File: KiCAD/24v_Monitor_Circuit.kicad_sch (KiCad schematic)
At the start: 2 parts, among them U3 PC365NJ0000F

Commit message: Ran Annotation and ERC
Annotated and ran Electronics Rules Checker. Started assigning footprints and appropriate step files to said footprints. Added custom KiCAD library folder to Github.
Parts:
- R17: renamed from R3; value R -> 2.28kΩ
- renumbered U3 to U10
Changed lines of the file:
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@@
   (symbol (lib_id "power:+24V") (at 111.76 76.2 0) (unit 1)
     (in_bom yes) (on_board yes) (dnp no) (fields_autoplaced)
-    (property "Reference" "#PWR011" (at 111.76 80.01 0)
+    (property "Reference" "#PWR020" (at 111.76 80.01 0)
       (effects (font (size 1.27 1.27)) hide)
     )
@@
       (project "ColletAutoFeed_RelayBoard"
         (path "/603d0a2e-fca7-40af-8fa8-51b59d823d4d/3e3ccaf3-28fc-483d-ba21-ff253f5b1972"
-          (reference "#PWR011") (unit 1)
+          (reference "#PWR020") (unit 1)
         )
       )
@@
   (symbol (lib_id "PC365NJ0000F:PC365NJ0000F") (at 133.35 92.71 0) (unit 1)
     (in_bom yes) (on_board yes) (dnp no) (fields_autoplaced)
-    (property "Reference" "U3" (at 133.35 77.47 0)
+    (property "Reference" "U10" (at 133.35 77.47 0)
       (effects (font (size 1.27 1.27)))
     )
@@
       (project "ColletAutoFeed_RelayBoard"
         (path "/603d0a2e-fca7-40af-8fa8-51b59d823d4d/3e3ccaf3-28fc-483d-ba21-ff253f5b1972"
-          (reference "U3") (unit 1)
+          (reference "U10") (unit 1)
         )
       )
@@
   (symbol (lib_id "Device:R") (at 111.76 106.68 0) (unit 1)
     (in_bom yes) (on_board yes) (dnp no) (fields_autoplaced)
-    (property "Reference" "R3" (at 114.3 105.41 0)
+    (property "Reference" "R17" (at 114.3 105.41 0)
       (effects (font (size 1.27 1.27)) (justify left))
     )
-    (property "Value" "R" (at 114.3 107.95 0)
+    (property "Value" "2.28kΩ" (at 114.3 107.95 0)
       (effects (font (size 1.27 1.27)) (justify left))
     )
@@
       (project "ColletAutoFeed_RelayBoard"
         (path "/603d0a2e-fca7-40af-8fa8-51b59d823d4d/3e3ccaf3-28fc-483d-ba21-ff253f5b1972"
-          (reference "R3") (unit 1)
+          (reference "R17") (unit 1)
         )
       )
@@
   (symbol (lib_id "power:GND") (at 111.76 113.03 0) (unit 1)
     (in_bom yes) (on_board yes) (dnp no) (fields_autoplaced)
-    (property "Reference" "#PWR012" (at 111.76 119.38 0)
+    (property "Reference" "#PWR021" (at 111.76 119.38 0)
       (effects (font (size 1.27 1.27)) hide)
     )
@@
       (project "ColletAutoFeed_RelayBoard"
         (path "/603d0a2e-fca7-40af-8fa8-51b59d823d4d/3e3ccaf3-28fc-483d-ba21-ff253f5b1972"
-          (reference "#PWR012") (unit 1)
+          (reference "#PWR021") (unit 1)
         )
       )

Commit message: Started PCB layout
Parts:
- R17: footprint (none) -> Resistor_THT:R_Axial_DIN0204_L3.6mm_D1.6mm_P5.08mm_Horizontal
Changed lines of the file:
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@@
       (effects (font (size 1.27 1.27)) (justify left))
     )
-    (property "Footprint" "" (at 109.982 106.68 90)
+    (property "Footprint" "Resistor_THT:R_Axial_DIN0204_L3.6mm_D1.6mm_P5.08mm_Horizontal" (at 109.982 106.68 90)
       (effects (font (size 1.27 1.27)) hide)
     )

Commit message: Changed to tht LEDs and added LED to power monitor circuit
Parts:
- added LED9: C503B-GCN-CY0C0792, CreeLED Green:C503B_GCN_CY0C0792, symbol CreeLED Green:C503B-GCN-CY0C0792
- added R18: 1.04kΩ, Resistor_THT:R_Axial_DIN0204_L3.6mm_D1.6mm_P5.08mm_Horizontal, symbol Device:R
- U10: footprint PC365NJ0000F:SOIC254P700X280-4N -> PC365NJ0000F:PC365NJ0000F
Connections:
- net +24V: now also LED9.2
- net GND: now also R18.2
- new net: LED9.1, R18.1
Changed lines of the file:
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@@
 (kicad_sch (version 20230121) (generator eeschema)
   (paper "A4")
+  (junction (at 111.76 110.49) (diameter 0) (color 0 0 0 0)
+  )
+  (junction (at 111.76 85.09) (diameter 0) (color 0 0 0 0)
+  )
+  (wire (pts (xy 96.52 85.09) (xy 111.76 85.09))
+    (stroke (width 0) (type default))
+  )
   (wire (pts (xy 148.59 85.09) (xy 160.02 85.09))
     (stroke (width 0) (type default))
   )
   (wire (pts (xy 111.76 76.2) (xy 111.76 85.09))
+    (stroke (width 0) (type default))
+  )
+  (wire (pts (xy 96.52 97.79) (xy 96.52 102.87))
+    (stroke (width 0) (type default))
+  )
+  (wire (pts (xy 96.52 110.49) (xy 111.76 110.49))
     (stroke (width 0) (type default))
   )
@@
   )
   (wire (pts (xy 111.76 85.09) (xy 118.11 85.09))
+    (stroke (width 0) (type default))
+  )
+  (wire (pts (xy 96.52 87.63) (xy 96.52 85.09))
     (stroke (width 0) (type default))
   )
@@
     )
   )
+  (symbol (lib_id "Device:R") (at 96.52 106.68 0) (unit 1)
+    (in_bom yes) (on_board yes) (dnp no) (fields_autoplaced)
+    (property "Reference" "R18" (at 99.06 105.41 0)
+      (effects (font (size 1.27 1.27)) (justify left))
+    )
+    (property "Value" "1.04kΩ" (at 99.06 107.95 0)
+      (effects (font (size 1.27 1.27)) (justify left))
+    )
+    (property "Footprint" "Resistor_THT:R_Axial_DIN0204_L3.6mm_D1.6mm_P5.08mm_Horizontal" (at 94.742 106.68 90)
+      (effects (font (size 1.27 1.27)) hide)
+    )
+    (property "Datasheet" "~" (at 96.52 106.68 0)
+      (effects (font (size 1.27 1.27)) hide)
+    )
+    (pin "2")
+    (pin "1")
+    (instances
+      (project "ColletAutoFeed_RelayBoard"
+        (path "/603d0a2e-fca7-40af-8fa8-51b59d823d4d/3e3ccaf3-28fc-483d-ba21-ff253f5b1972"
+          (reference "R18") (unit 1)
+        )
+      )
+    )
+  )
   (symbol (lib_id "PC365NJ0000F:PC365NJ0000F") (at 133.35 92.71 0) (unit 1)
     (in_bom yes) (on_board yes) (dnp no) (fields_autoplaced)
@@
       (effects (font (size 1.27 1.27)))
     )
-    (property "Footprint" "PC365NJ0000F:SOIC254P700X280-4N" (at 133.35 92.71 0)
+    (property "Footprint" "PC365NJ0000F:PC365NJ0000F" (at 133.35 92.71 0)
       (effects (font (size 1.27 1.27)) (justify bottom) hide)
     )
@@
       (effects (font (size 1.27 1.27)) (justify bottom) hide)
     )
-    (pin "1")
+    (pin "2")
     (pin "4")
     (pin "3")
-    (pin "2")
+    (pin "1")
     (instances
       (project "ColletAutoFeed_RelayBoard"
@@
         )
       )
+    )
+  )
+  (symbol (lib_id "CreeLED Green:C503B-GCN-CY0C0792") (at 96.52 87.63 270) (unit 1)
+    (in_bom yes) (on_board yes) (dnp no)
+    (property "Reference" "LED9" (at 93.98 91.44 90)
+      (effects (font (size 1.524 1.524)) (justify right))
+    )
+    (property "Value" "C503B-GCN-CY0C0792" (at 93.98 93.98 90)
+      (effects (font (size 1.524 1.524)) (justify right))
+    )
+    (property "Footprint" "CreeLED Green:C503B_GCN_CY0C0792" (at 96.52 87.63 0)
+      (effects (font (size 1.27 1.27) italic) hide)
+    )
+    (property "Datasheet" "C503B-GCN-CY0C0792" (at 96.52 87.63 0)
+      (effects (font (size 1.27 1.27) italic) hide)
+    )
+    (pin "1")
+    (pin "2")
+    (instances
+      (project "ColletAutoFeed_RelayBoard"
+        (path "/603d0a2e-fca7-40af-8fa8-51b59d823d4d/3e3ccaf3-28fc-483d-ba21-ff253f5b1972"
+          (reference "LED9") (unit 1)
+        )
+      )

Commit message: Updated resistor footprints to include values
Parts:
- R17, R18: footprint Resistor_THT:R_Axial_DIN0204_L3.6mm_D1.6mm_P5.08mm_Horizontal -> Resistor:R_Axial_DIN0204_L3.6mm_D1.6mm_P5.08mm_Horizontal-JW
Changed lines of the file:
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@@
       (effects (font (size 1.27 1.27)) (justify left))
     )
-    (property "Footprint" "Resistor_THT:R_Axial_DIN0204_L3.6mm_D1.6mm_P5.08mm_Horizontal" (at 94.742 106.68 90)
+    (property "Footprint" "Resistor:R_Axial_DIN0204_L3.6mm_D1.6mm_P5.08mm_Horizontal-JW" (at 94.742 106.68 90)
       (effects (font (size 1.27 1.27)) hide)
     )
@@
       (effects (font (size 1.27 1.27)) (justify left))
     )
-    (property "Footprint" "Resistor_THT:R_Axial_DIN0204_L3.6mm_D1.6mm_P5.08mm_Horizontal" (at 109.982 106.68 90)
+    (property "Footprint" "Resistor:R_Axial_DIN0204_L3.6mm_D1.6mm_P5.08mm_Horizontal-JW" (at 109.982 106.68 90)
       (effects (font (size 1.27 1.27)) hide)
     )

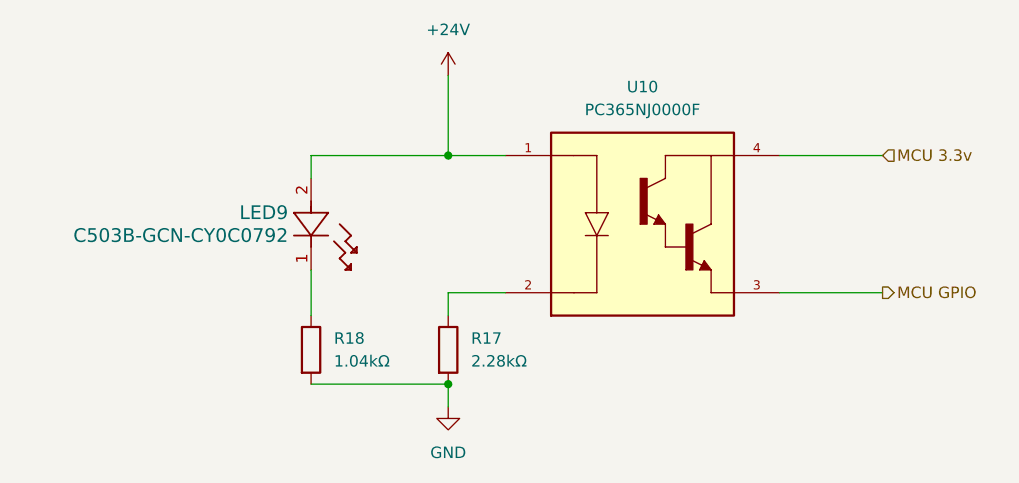
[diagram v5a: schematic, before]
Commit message: Replaced remaining opto-isolator and started silkscreen
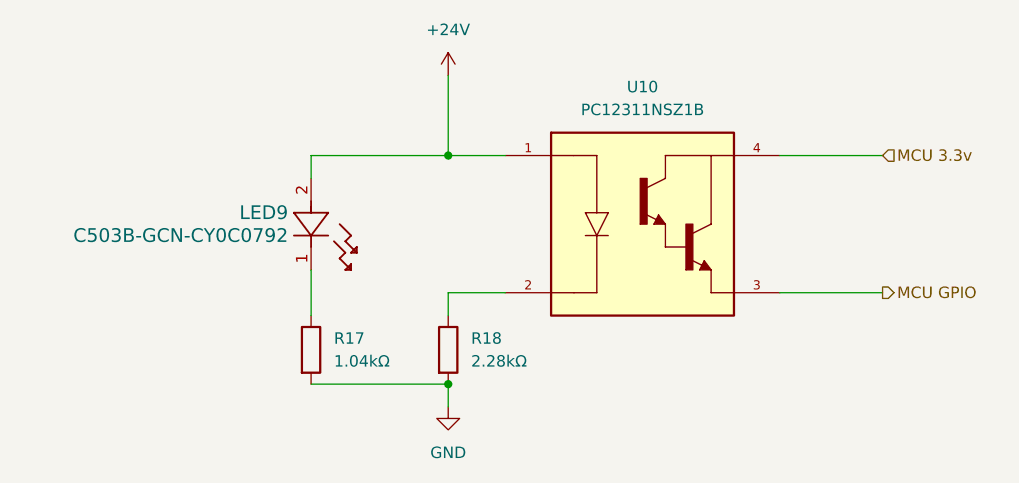
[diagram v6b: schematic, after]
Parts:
- removed U10: PC365NJ0000F, PC365NJ0000F:PC365NJ0000F, symbol PC365NJ0000F:PC365NJ0000F
- added U10: PC12311NSZ1B, PC12311NSZ1B:PC12311NSZ1B, symbol PC12311NSZ1B:PC12311NSZ1B
- renumbered R18 to R17, R17 to R18
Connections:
- net +24V: now also U10.1
- net MCU 3.3v: now also U10.4
- net MCU GPIO: now also U10.3
- net at R18.1: now also U10.2
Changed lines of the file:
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@@
   (symbol (lib_id "power:+24V") (at 111.76 76.2 0) (unit 1)
     (in_bom yes) (on_board yes) (dnp no) (fields_autoplaced)
-    (property "Reference" "#PWR020" (at 111.76 80.01 0)
+    (property "Reference" "#PWR019" (at 111.76 80.01 0)
       (effects (font (size 1.27 1.27)) hide)
     )
@@
       (project "ColletAutoFeed_RelayBoard"
         (path "/603d0a2e-fca7-40af-8fa8-51b59d823d4d/3e3ccaf3-28fc-483d-ba21-ff253f5b1972"
-          (reference "#PWR020") (unit 1)
+          (reference "#PWR019") (unit 1)
+        )
+      )
+    )
+  )
+  (symbol (lib_id "PC12311NSZ1B:PC12311NSZ1B") (at 134.62 93.98 0) (unit 1)
+    (in_bom yes) (on_board yes) (dnp no) (fields_autoplaced)
+    (property "Reference" "U10" (at 133.35 77.47 0)
+      (effects (font (size 1.27 1.27)))
+    )
+    (property "Value" "PC12311NSZ1B" (at 133.35 80.01 0)
+      (effects (font (size 1.27 1.27)))
+    )
+    (property "Footprint" "PC12311NSZ1B:PC12311NSZ1B" (at 151.13 188.9 0)
+      (effects (font (size 1.27 1.27)) (justify left top) hide)
+    )
+    (property "Datasheet" "https://datasheet.datasheetarchive.com/originals/distributors/Datasheets_SAMA/562baaf804994183fb5e18c5f5c92935.pdf" (at 151.13 288.9 0)
+      (effects (font (size 1.27 1.27)) (justify left top) hide)
+    )
+    (property "Height" "4.45" (at 151.13 488.9 0)
+      (effects (font (size 1.27 1.27)) (justify left top) hide)
+    )
+    (property "Mouser Part Number" "852-PC12311NSZ1B" (at 151.13 588.9 0)
+      (effects (font (size 1.27 1.27)) (justify left top) hide)
+    )
+    (property "Mouser Price/Stock" "https://www.mouser.co.uk/ProductDetail/Sharp-Microelectronics/PC12311NSZ1B?qs=0lSvoLzn4L8JFTcuQxvmTA%3D%3D" (at 151.13 688.9 0)
+      (effects (font (size 1.27 1.27)) (justify left top) hide)
+    )
+    (property "Manufacturer_Name" "Sharp Microelectronics" (at 151.13 788.9 0)
+      (effects (font (size 1.27 1.27)) (justify left top) hide)
+    )
+    (property "Manufacturer_Part_Number" "PC12311NSZ1B" (at 151.13 888.9 0)
+      (effects (font (size 1.27 1.27)) (justify left top) hide)
+    )
+    (pin "1")
+    (pin "2")
+    (pin "3")
+    (pin "4")
+    (instances
+      (project "ColletAutoFeed_RelayBoard"
+        (path "/603d0a2e-fca7-40af-8fa8-51b59d823d4d/3e3ccaf3-28fc-483d-ba21-ff253f5b1972"
+          (reference "U10") (unit 1)
         )
       )
@@
   (symbol (lib_id "Device:R") (at 96.52 106.68 0) (unit 1)
     (in_bom yes) (on_board yes) (dnp no) (fields_autoplaced)
-    (property "Reference" "R18" (at 99.06 105.41 0)
+    (property "Reference" "R17" (at 99.06 105.41 0)
       (effects (font (size 1.27 1.27)) (justify left))
     )
@@
       (project "ColletAutoFeed_RelayBoard"
         (path "/603d0a2e-fca7-40af-8fa8-51b59d823d4d/3e3ccaf3-28fc-483d-ba21-ff253f5b1972"
-          (reference "R18") (unit 1)
-        )
-      )
-    )
-  )
-  (symbol (lib_id "PC365NJ0000F:PC365NJ0000F") (at 133.35 92.71 0) (unit 1)
-    (in_bom yes) (on_board yes) (dnp no) (fields_autoplaced)
-    (property "Reference" "U10" (at 133.35 77.47 0)
-      (effects (font (size 1.27 1.27)))
-    )
-    (property "Value" "PC365NJ0000F" (at 133.35 80.01 0)
-      (effects (font (size 1.27 1.27)))
-    )
-    (property "Footprint" "PC365NJ0000F:PC365NJ0000F" (at 133.35 92.71 0)
-      (effects (font (size 1.27 1.27)) (justify bottom) hide)
-    )
-    (property "Datasheet" "" (at 133.35 92.71 0)
-      (effects (font (size 1.27 1.27)) hide)
-    )
-    (property "PARTREV" "Jun. 30. 2005" (at 133.35 92.71 0)
-      (effects (font (size 1.27 1.27)) (justify bottom) hide)
-    )
-    (property "MANUFACTURER" "Sharp" (at 133.35 92.71 0)
-      (effects (font (size 1.27 1.27)) (justify bottom) hide)
-    )
-    (property "MAXIMUM_PACKAGE_HEIGHT" "2.80mm" (at 133.35 92.71 0)
-      (effects (font (size 1.27 1.27)) (justify bottom) hide)
-    )
-    (property "STANDARD" "IPC-7351B" (at 133.35 92.71 0)
-      (effects (font (size 1.27 1.27)) (justify bottom) hide)
-    )
-    (pin "2")
-    (pin "4")
-    (pin "3")
-    (pin "1")
-    (instances
-      (project "ColletAutoFeed_RelayBoard"
-        (path "/603d0a2e-fca7-40af-8fa8-51b59d823d4d/3e3ccaf3-28fc-483d-ba21-ff253f5b1972"
-          (reference "U10") (unit 1)
+          (reference "R17") (unit 1)
         )
       )
@@
   (symbol (lib_id "Device:R") (at 111.76 106.68 0) (unit 1)
     (in_bom yes) (on_board yes) (dnp no) (fields_autoplaced)
-    (property "Reference" "R17" (at 114.3 105.41 0)
+    (property "Reference" "R18" (at 114.3 105.41 0)
       (effects (font (size 1.27 1.27)) (justify left))
     )
@@
       (project "ColletAutoFeed_RelayBoard"
         (path "/603d0a2e-fca7-40af-8fa8-51b59d823d4d/3e3ccaf3-28fc-483d-ba21-ff253f5b1972"
-          (reference "R17") (unit 1)
+          (reference "R18") (unit 1)
         )
       )
@@
   (symbol (lib_id "power:GND") (at 111.76 113.03 0) (unit 1)
     (in_bom yes) (on_board yes) (dnp no) (fields_autoplaced)
-    (property "Reference" "#PWR021" (at 111.76 119.38 0)
+    (property "Reference" "#PWR020" (at 111.76 119.38 0)
       (effects (font (size 1.27 1.27)) hide)
     )
@@
       (project "ColletAutoFeed_RelayBoard"
         (path "/603d0a2e-fca7-40af-8fa8-51b59d823d4d/3e3ccaf3-28fc-483d-ba21-ff253f5b1972"
-          (reference "#PWR021") (unit 1)
+          (reference "#PWR020") (unit 1)
         )
       )

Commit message: Fixed Silkscreen Labels for Components
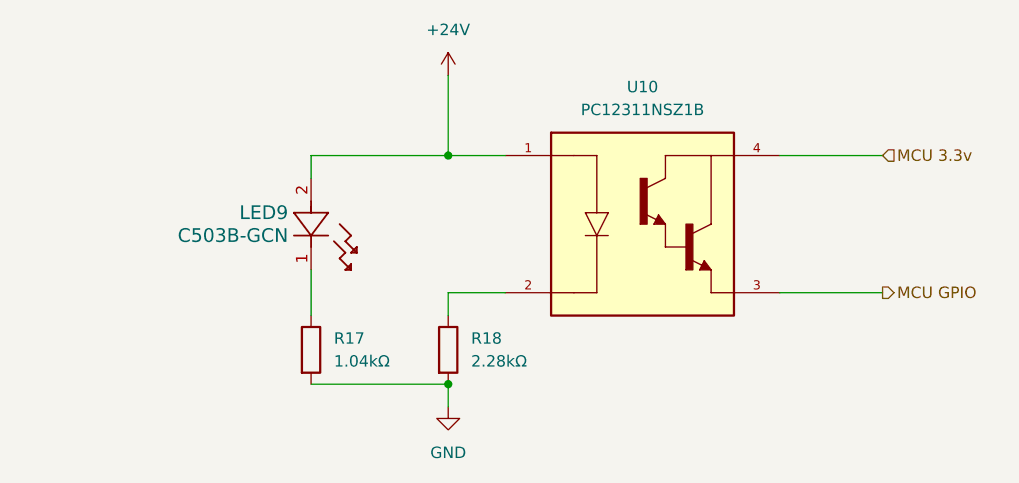
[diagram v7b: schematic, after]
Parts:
- LED9: value C503B-GCN-CY0C0792 -> C503B-GCN
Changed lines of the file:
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@@
       (effects (font (size 1.524 1.524)) (justify right))
     )
-    (property "Value" "C503B-GCN-CY0C0792" (at 93.98 93.98 90)
+    (property "Value" "C503B-GCN" (at 93.98 93.98 90)
       (effects (font (size 1.524 1.524)) (justify right))
     )
